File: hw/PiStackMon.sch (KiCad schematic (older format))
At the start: 61 parts, among them J1 Conn_01x03, J10 Conn_01x02, J2 Conn_01x03, J3 Screw_Terminal_01x02, J4 Screw_Terminal_01x02, J5 Conn_01x02, J6 Conn_01x02, J7 Conn_01x07, J8 Conn_01x05, J9 Conn_01x03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

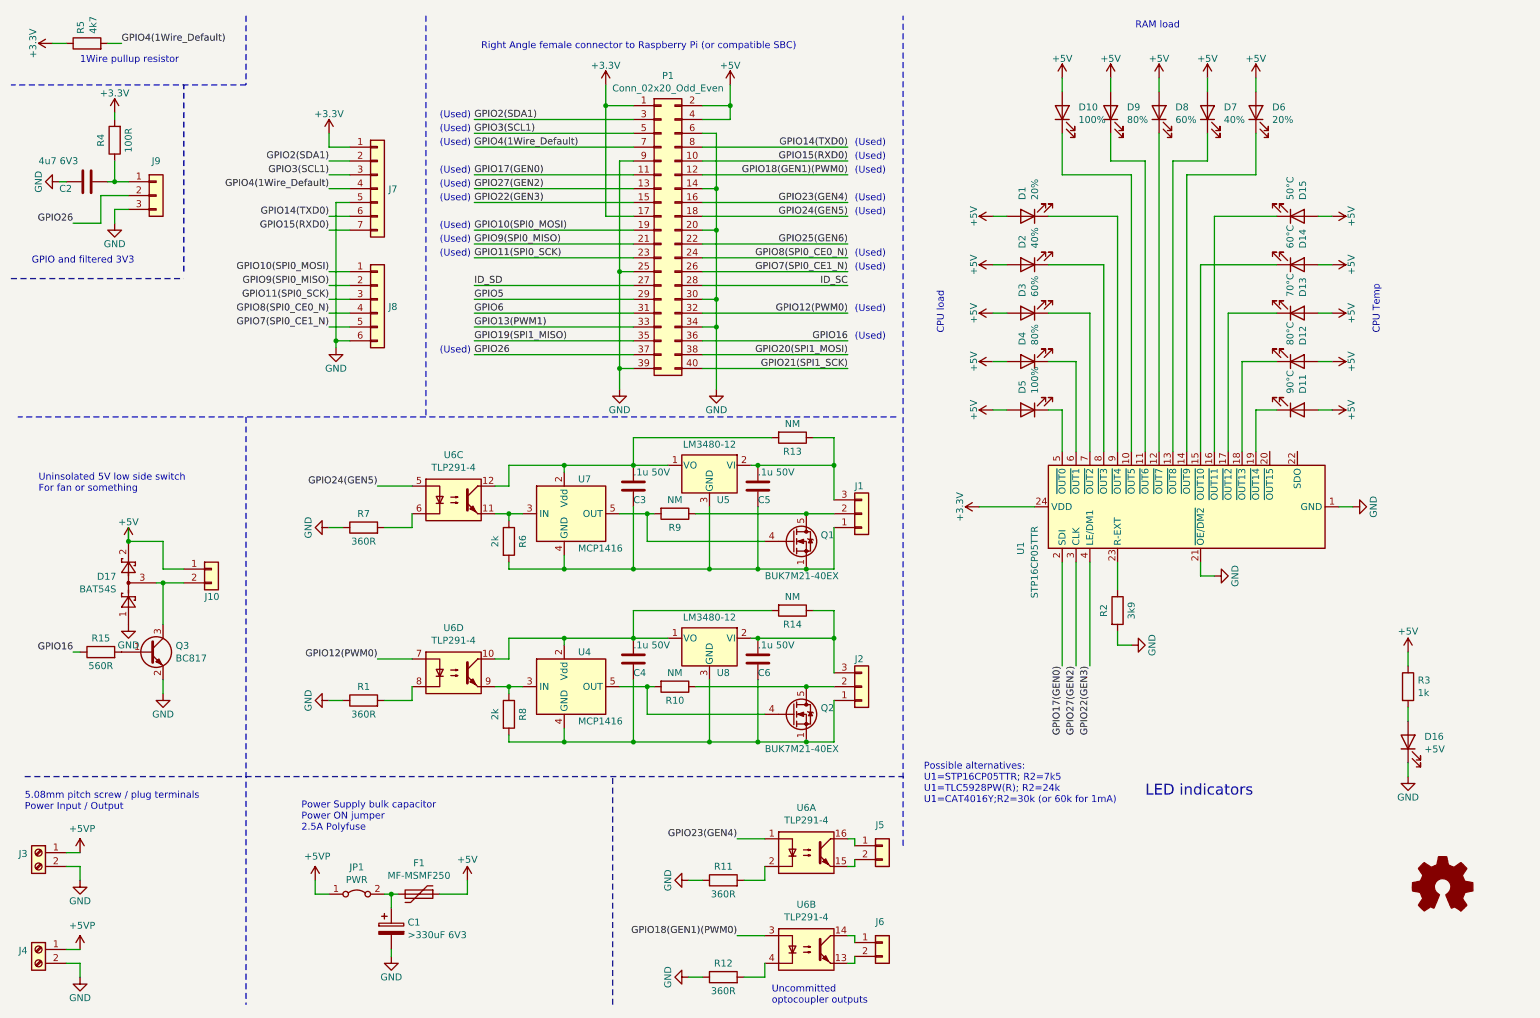
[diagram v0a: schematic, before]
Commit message: More alt components; JLC assembly component codes
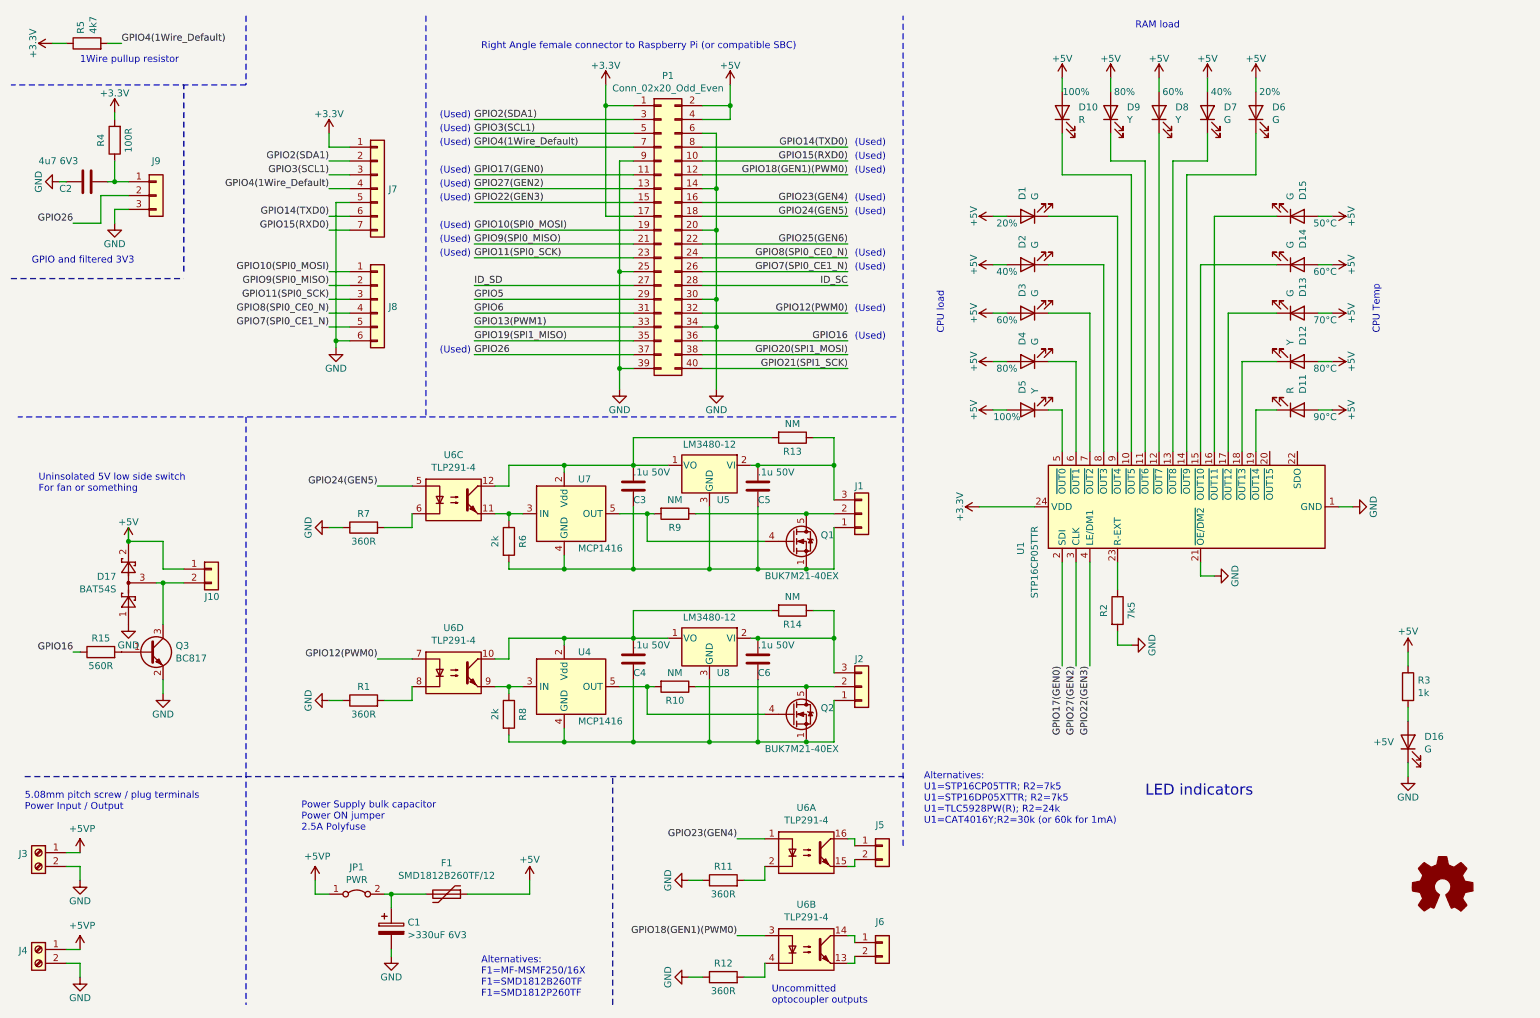
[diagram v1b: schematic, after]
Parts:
- C2: LCSC (none) -> C8032
- C3, C4, C5, C6: LCSC (none) -> C14663
- D1, D6: value 20% -> G; Comment (none) -> 20%; LCSC (none) -> C72043
- D10: value 100% -> R; Comment (none) -> 100%; LCSC (none) -> C72044
- D11: value 90°C -> R; Comment (none) -> 90°C; LCSC (none) -> C72044
- D12: value 80°C -> Y; Comment (none) -> 80°C; LCSC (none) -> C72038
- D13: value 70°C -> G; Comment (none) -> 70°C; LCSC (none) -> C72043
- D14: value 60°C -> G; Comment (none) -> 60°C; LCSC (none) -> C72043
- D15: value 50°C -> G; Comment (none) -> 50°C; LCSC (none) -> C72043
- D16: value +5V -> G; Comment (none) -> +5V; LCSC (none) -> C72043
- D17: LCSC (none) -> C47546
- D2, D7: value 40% -> G; Comment (none) -> 40%; LCSC (none) -> C72043
- D3: value 60% -> G; Comment (none) -> 60%; LCSC (none) -> C72043
- D4: value 80% -> G; Comment (none) -> 80%; LCSC (none) -> C72043
- D5: value 100% -> Y; Comment (none) -> 100%; LCSC (none) -> C72038
- D8: value 60% -> Y; Comment (none) -> 60%; LCSC (none) -> C72038
- D9: value 80% -> Y; Comment (none) -> 80%; LCSC (none) -> C72038
- F1: value MF-MSMF250 -> SMD1812B260TF/12; LCSC (none) -> C269147
- Q3: LCSC (none) -> C52801
- R1, R11, R12, R7: LCSC (none) -> C25194
- R15: LCSC (none) -> C23204
- R2: value 3k9 -> 7k5; LCSC (none) -> C23234
- R3: LCSC (none) -> C21190
- R4: LCSC (none) -> C22775
- R5: LCSC (none) -> C23162
- R6, R8: LCSC (none) -> C22975
- U1: LCSC (none) -> C127267
- U4, U7: LCSC (none) -> C83775
- U5, U8: LCSC (none) -> C130175
- U6: LCSC (none) -> C60900
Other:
- note added: "Alternatives:\nF1=MF-MSMF250/16X\nF1=SMD1812B260TF\nF1=SMD1812P260TF"
- note added: "Alternatives:\nU1=STP16CP05TTR; R2=7k5\nU1=STP16DP05XTTR; R2=7k5\nU1=TLC5928PW(R); R2=24k\nU1=CAT4016Y;R2=30k (or 60k for 1mA)"
- note removed: "Possible alternatives:\nU1=STP16CP05TTR; R2=7k5\nU1=TLC5928PW(R); R2=24k\nU1=CAT4016Y;R2=30k (or 60k for 1mA)"
- moved on the sheet: F1

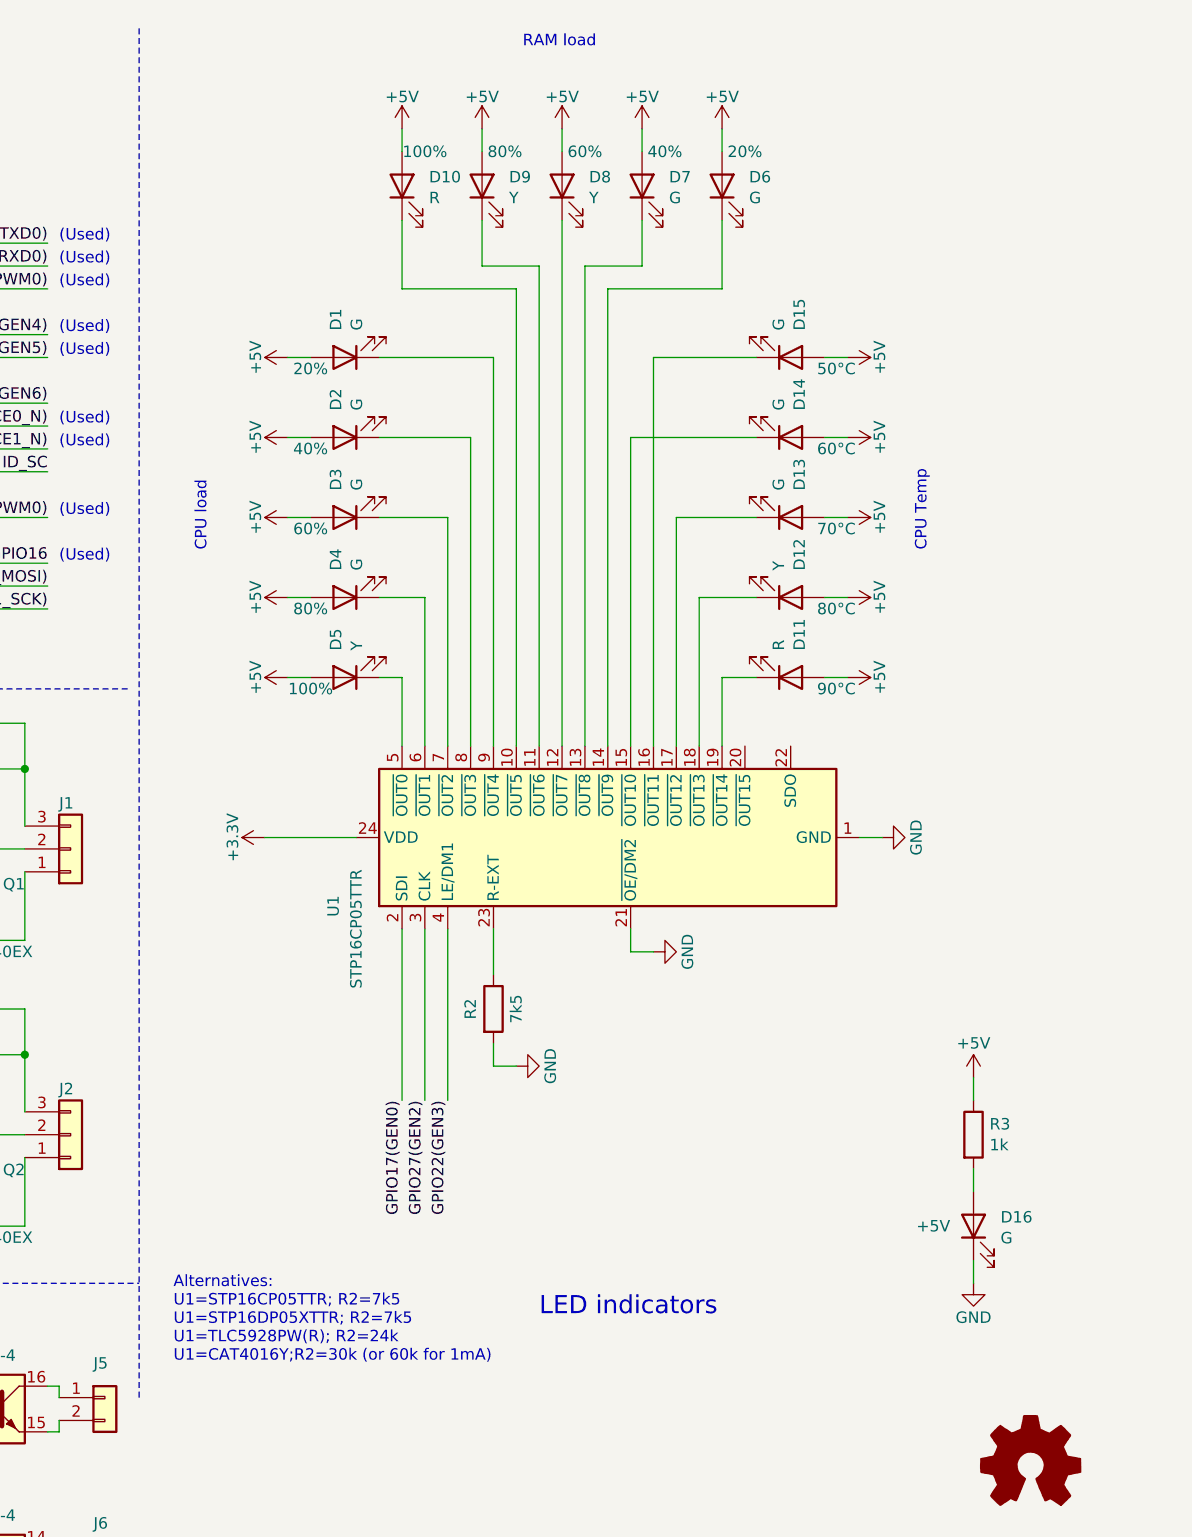
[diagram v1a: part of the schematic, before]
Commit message: Colors of some LEDs changed; More information about adjusting LED currents
Temperature monitor LEDs have been changed to reflect 70 deg as a warning temperature (yellow), since some RPi models apply soft throttling above 60 deg. Also running Pi at 70 deg and beyond is probably a bad idea in general (hence red LEDs over 70 deg).
RAM indicator sees color change to green at 60% level, since this is not really a state worth warning just yet.

More R2 values are provided on the schematic to let the user pick all sorts of LED currents.
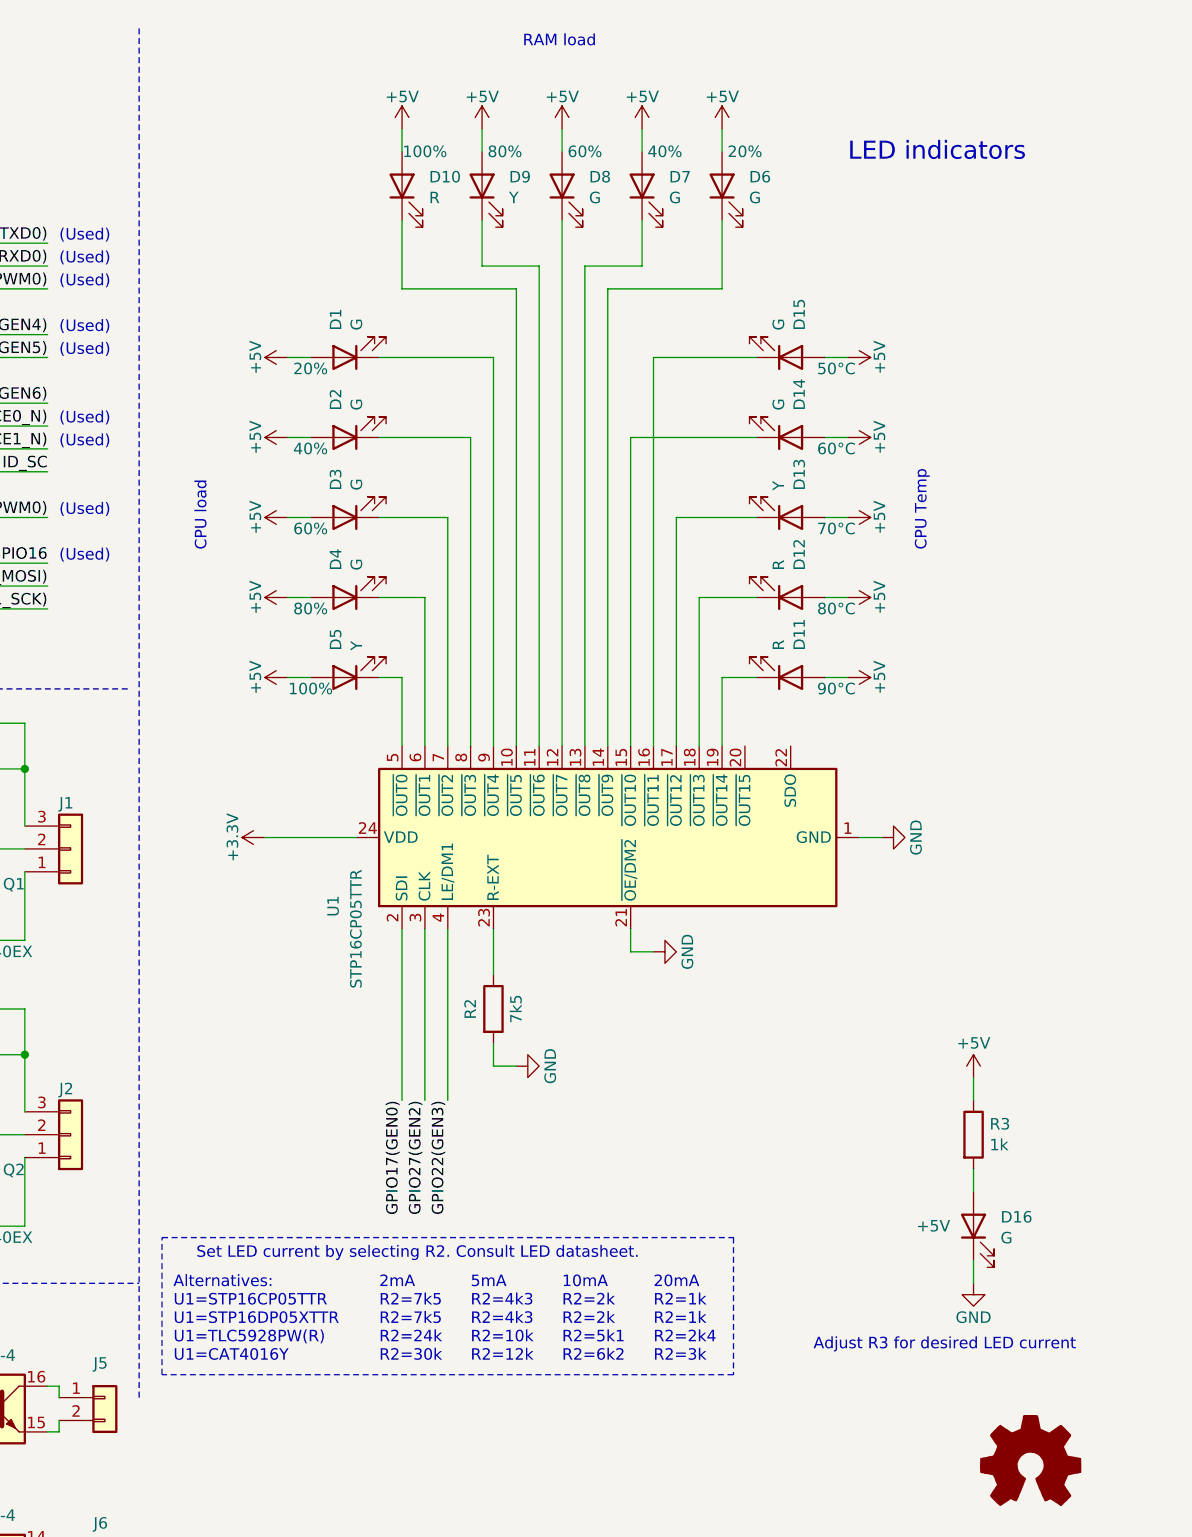
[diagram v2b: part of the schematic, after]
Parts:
- D12: value Y -> R
- D13: value G -> Y
- D8: value Y -> G
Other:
- note added: "10mA\nR2=2k\nR2=2k\nR2=5k1\nR2=6k2"
- note added: "20mA\nR2=1k\nR2=1k\nR2=2k4\nR2=3k"
- note added: "2mA\nR2=7k5\nR2=7k5\nR2=24k\nR2=30k"
- note added: "5mA\nR2=4k3\nR2=4k3\nR2=10k\nR2=12k"
- note added: "Adjust R3 for desired LED current"
- note added: "Alternatives:\nU1=STP16CP05TTR\nU1=STP16DP05XTTR\nU1=TLC5928PW(R)\nU1=CAT4016Y"
- note added: "Set LED current by selecting R2. Consult LED datasheet."
- note removed: "Alternatives:\nU1=STP16CP05TTR; R2=7k5\nU1=STP16DP05XTTR; R2=7k5\nU1=TLC5928PW(R); R2=24k\nU1=CAT4016Y;R2=30k (or 60k for 1mA)"
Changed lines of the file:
@@
 Text Notes 2600 6450 0    50   ~ 0
 Power Supply bulk capacitor\nPower ON jumper \n2.5A Polyfuse
-Text Notes 8700 6200 0    79   ~ 0
+Text Notes 10050 1150 0    79   ~ 0
 LED indicators
 Wire Notes Line
@@
 P 8800 1250
 F 0 "D8" V 8839 1132 50  0000 R CNN
-F 1 "Y" V 8748 1132 50  0000 R CNN
+F 1 "G" V 8748 1132 50  0000 R CNN
 F 2 "LED_SMD:LED_0603_1608Metric_Pad1.05x0.95mm_HandSolder" H 8800 1250 50  0001 C CNN
 F 3 "~" H 8800 1250 50  0001 C CNN
@@
 P 9800 3050
 F 0 "D12" V 9839 2932 50  0000 R CNN
-F 1 "Y" V 9748 2932 50  0000 R CNN
+F 1 "R" V 9748 2932 50  0000 R CNN
 F 2 "LED_SMD:LED_0603_1608Metric_Pad1.05x0.95mm_HandSolder" H 9800 3050 50  0001 C CNN
 F 3 "~" H 9800 3050 50  0001 C CNN
@@
 P 9800 2700
 F 0 "D13" V 9839 2582 50  0000 R CNN
-F 1 "G" V 9748 2582 50  0000 R CNN
+F 1 "Y" V 9748 2582 50  0000 R CNN
 F 2 "LED_SMD:LED_0603_1608Metric_Pad1.05x0.95mm_HandSolder" H 9800 2700 50  0001 C CNN
 F 3 "~" H 9800 2700 50  0001 C CNN
@@
 	3250 6900 3500 6900
 Text Notes 7100 6400 0    50   ~ 0
-Alternatives:\nU1=STP16CP05TTR; R2=7k5\nU1=STP16DP05XTTR; R2=7k5\nU1=TLC5928PW(R); R2=24k\nU1=CAT4016Y;R2=30k (or 60k for 1mA)
+Alternatives:\nU1=STP16CP05TTR\nU1=STP16DP05XTTR\nU1=TLC5928PW(R)\nU1=CAT4016Y
 Text Notes 3900 7650 0    50   ~ 0
 Alternatives:\nF1=MF-MSMF250/16X\nF1=SMD1812B260TF\nF1=SMD1812P260TF
 Wire Wire Line
 	3800 6900 4250 6900
+Text Notes 8000 6400 0    50   ~ 0
+2mA\nR2=7k5\nR2=7k5\nR2=24k\nR2=30k
+Text Notes 7200 5950 0    50   ~ 0
+Set LED current by selecting R2. Consult LED datasheet.
+Text Notes 8400 6400 0    50   ~ 0
+5mA\nR2=4k3\nR2=4k3\nR2=10k\nR2=12k
+Text Notes 8800 6400 0    50   ~ 0
+10mA\nR2=2k\nR2=2k\nR2=5k1\nR2=6k2
+Text Notes 9200 6400 0    50   ~ 0
+20mA\nR2=1k\nR2=1k\nR2=2k4\nR2=3k
+Text Notes 9900 6350 0    50   ~ 0
+Adjust R3 for desired LED current
+Wire Notes Line
+	7050 5850 9550 5850
+Wire Notes Line
+	9550 5850 9550 6450
+Wire Notes Line
+	9550 6450 7050 6450
+Wire Notes Line
+	7050 6450 7050 5850
 $EndSCHEMATC
